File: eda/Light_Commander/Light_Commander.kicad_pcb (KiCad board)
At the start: 2 copper layers, 71 x 108 mm, 164 parts, among them J1 GATE0, J10 BUFFB, J11 BUFFC, J12 BUFFD, J13 Eurorack_Power, J14 USB_C_Receptacle_USB2.0_16P, J15 Conn_01x05, J16 MIDI_IN, J17 MIDI_THRU, J18 Conn_01x03, J19 Conn_02x07_Odd_Even, J2 GATE1, J20 Conn_02x03_Odd_Even, J3 GATE2, J4 GATE3, J5 INA, J6 INB, J7 INC, J8 IND, J9 BUFFA, Q1 MMBT3904, Q2 MMBT3904, Q3 MMBT3904, Q4 MMBT3904, Q5 Q_PMOS_GSD, Q6 Q_NMOS_GSD, Q7 Q_PMOS_GDS, SW1 RotaryEncoder_Switch, SW2 SW_Push, SW3 SW_DPDT_x2, SW4 SW_DPDT_x2, U1 STM32F446RETx, U10 6N137, U11 NXU0101GW, U2 TL084, U3 AD8544, U4 R-785.0-0.5, U5 AP2112K-3.3, U6 USBLC6-2SC6, U7 2.5V Ref, U8 NXU0101GW, U9 SH1106_OLED, Y1 8 MHz

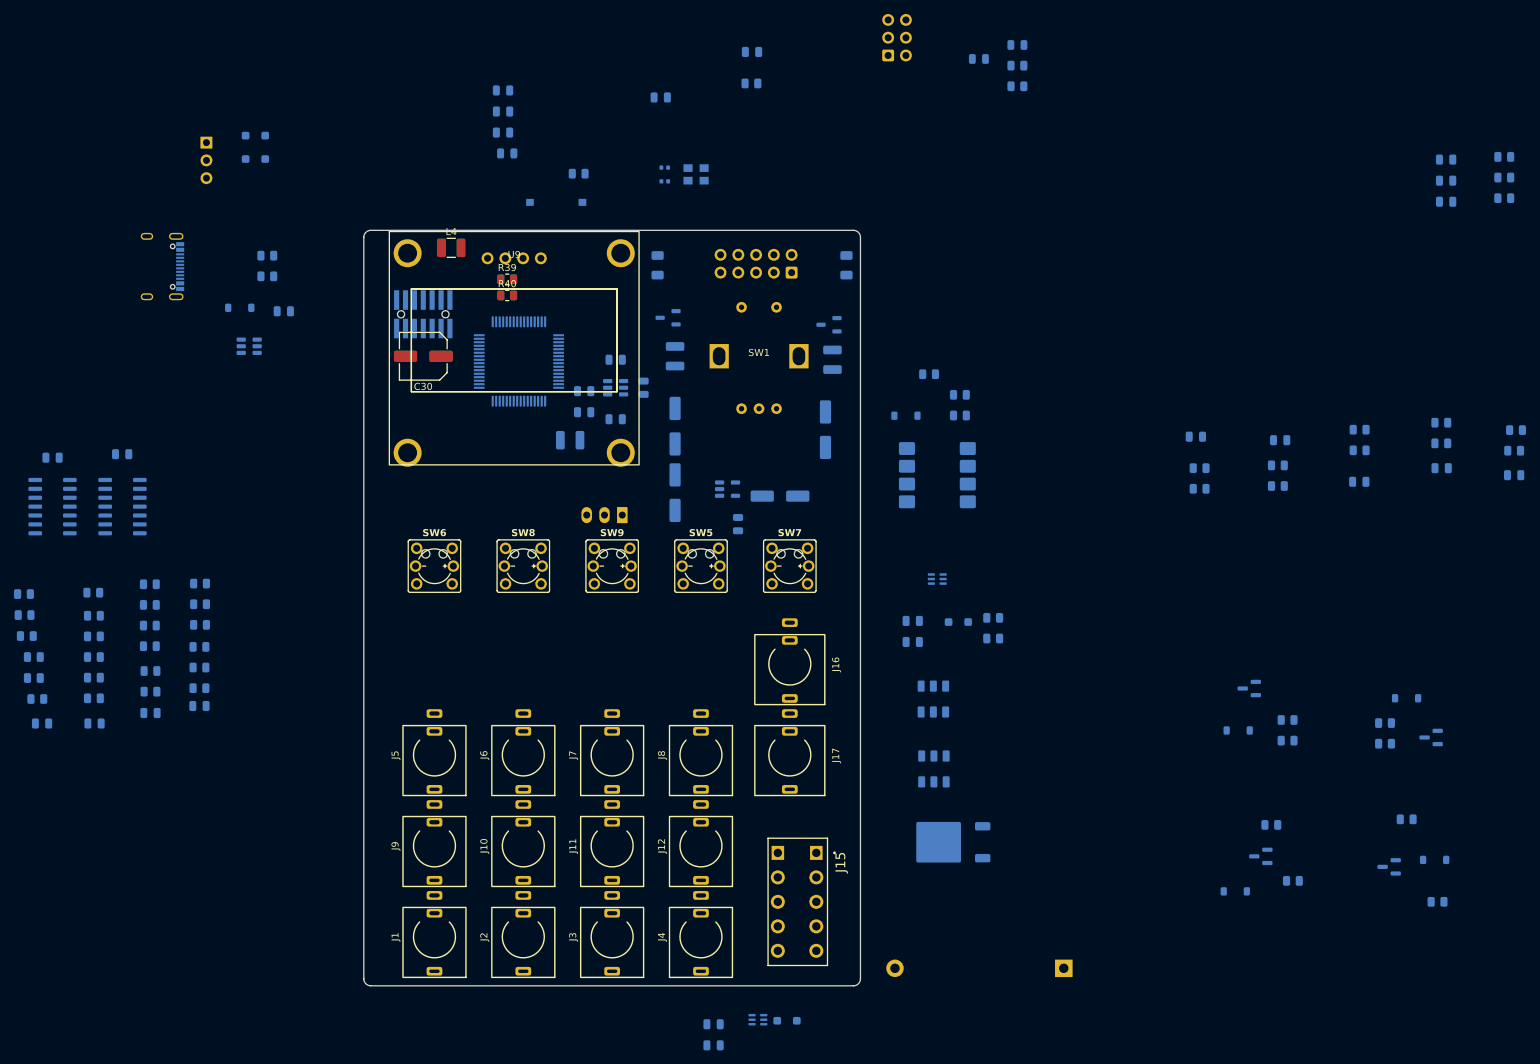
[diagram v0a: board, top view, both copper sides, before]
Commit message: Initial component placement
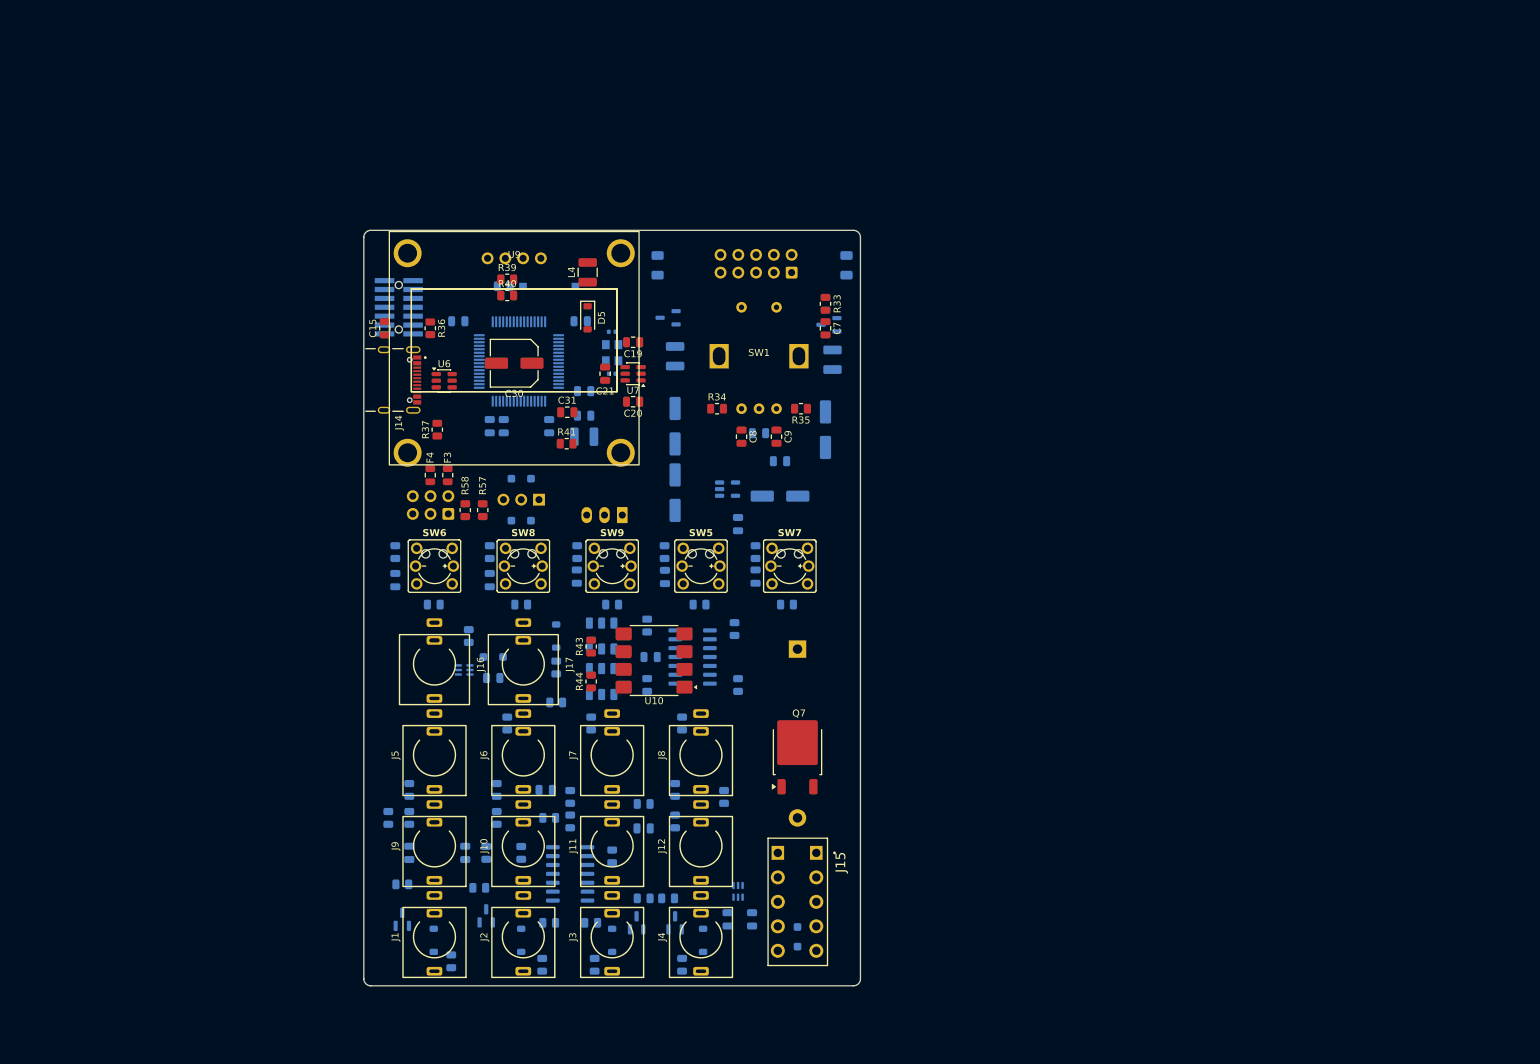
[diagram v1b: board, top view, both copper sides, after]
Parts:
- C15, C19, C20, C21, C31, C7, C8, C9, D5, F3, F4, J14, Q7, R33, R34, R35, R36, R37, R41, R43, R44, R57, R58, U10, U6, U7: moved to F.Cu
- moved Q1 149.4 mm to (70.0, 144.5), turned to 90 degrees
- moved D1 143.3 mm to (74.5, 147.5), turned to 90 degrees
- moved R26 141.9 mm to (70.0, 139.5), turned to 0 degrees
- moved R25 137.8 mm to (77.0, 150.5), turned to 90 degrees
- moved R30 120.8 mm to (97.5, 151.0), turned to 90 degrees
- moved D4 118.1 mm to (100.0, 147.5), turned to 90 degrees
- moved R28 117.5 mm to (81.0, 140.0), turned to 0 degrees
- moved R34 117.3 mm to (115.0, 71.5), turned to 0 degrees
- moved C35 116.3 mm to (69.0, 96.0), turned to -90 degrees
- moved R50 115.3 mm to (69.0, 92.0), turned to 90 degrees
- moved C37 114.8 mm to (82.5, 96.0), turned to -90 degrees
- moved Q2 113.8 mm to (82.0, 144.0), turned to 90 degrees
- moved R54 113.1 mm to (82.5, 92.0), turned to 90 degrees
- moved R56 112.8 mm to (95.0, 92.0), turned to 90 degrees
- moved C38 112.7 mm to (95.0, 95.5), turned to -90 degrees
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
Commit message: Start of trace routing
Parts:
- moved D5 23.8 mm to (76.0, 70.5), turned to 180 degrees
- moved C1 9.49 mm to (68.0, 126.0), turned to 90 degrees
- moved C2 9.22 mm to (81.0, 126.0), turned to 90 degrees
- moved R57 9.01 mm to (73.0, 89.0), turned to 0 degrees
- moved C21 7.50 mm to (106.5, 66.5)
- moved R9 5.22 mm to (83.5, 130.0)
- moved R42 4.27 mm to (93.5, 104.5), turned to 90 degrees
- moved C17 3.61 mm to (97.0, 64.5), turned to 180 degrees
- moved R40 3.50 mm to (88.5, 55.3)
- moved R23 3.20 mm to (107.0, 126.0), turned to 90 degrees
- moved C4 2.69 mm to (107.0, 130.5), turned to -90 degrees
- moved R11 2.50 mm to (81.0, 130.0)
- moved R45 2.00 mm to (81.5, 104.0)
- moved R41 1.58 mm to (93.0, 75.0), turned to 90 degrees
- moved Q6 1.05 mm to (132.1, 59.5), turned to 90 degrees
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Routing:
- net GND: track 0.00 -> 127.6 mm, vias 0 -> 51
- net +2V5: track 0.00 -> 107.6 mm, vias 0 -> 5
- net +3V3: track 0.00 -> 78.0 mm, vias 0 -> 23
- net Net-(U3A-+): track 0.00 -> 59.6 mm, vias 0 -> 1
- net Net-(U3B-+): track 0.00 -> 53.8 mm, vias 0 -> 2
- net INA_JACK: track 0.00 -> 41.0 mm, vias 0 -> 1
- net Net-(U3C-+): track 0.00 -> 40.1 mm, vias 0 -> 2
- net Net-(SW3A-C): track 0.00 -> 35.7 mm, vias 0 -> 2
- net I2C_SDA_EXPANDER: track 0.00 -> 34.6 mm
- net INC_JACK: track 0.00 -> 33.1 mm, vias 0 -> 1
- net BUFFA_JACK: track 0.00 -> 32.7 mm
- net INB_JACK: track 0.00 -> 32.5 mm, vias 0 -> 1
- net BUFFD_JACK: track 0.00 -> 31.6 mm
- net Net-(U3D-+): track 0.00 -> 30.6 mm, vias 0 -> 2
- net Net-(SW3A-A): track 0.00 -> 29.2 mm
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- added copper zone on In2.Cu, net +3V3
- added copper zone on F.Cu, net GND
- added copper zone on In1.Cu, net GND
- added copper zone on In2.Cu, net GND
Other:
- copper layers 2 -> 4

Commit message: More routing
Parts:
- R47, R49, R51, R53, R55: moved to F.Cu
- moved R47 7.85 mm to (118.1, 94.0), turned to 90 degrees
- moved R51 7.78 mm to (130.5, 94.0), turned to 90 degrees
- moved R53 7.71 mm to (92.4, 94.0), turned to 90 degrees
- moved R49 7.50 mm to (79.6, 94.0), turned to 90 degrees
- moved R55 7.43 mm to (105.0, 94.0), turned to 90 degrees
- moved U4 1.21 mm to (101.4, 85.5)
- moved R18 0.50 mm to (118.0, 103.0)
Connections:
- U1 pad 2: unconnected-(U1-PC13-Pad2) -> MIDI_BTN
- U1 pad 23: unconnected-(U1-PA7-Pad23) -> BACK_BTN
- U1 pad 27: unconnected-(U1-PB1-Pad27) -> MIDI_LED
- U1 pad 28: unconnected-(U1-PB2-Pad28) -> SETTINGS_LED
- U1 pad 33: unconnected-(U1-PB12-Pad33) -> FX_CHANGE_LED
- U1 pad 34: unconnected-(U1-PB13-Pad34) -> MOD_LED
- U1 pad 35: unconnected-(U1-PB14-Pad35) -> BACK_LED
- U1 pad 43: unconnected-(U1-PA10-Pad43) -> FX_CHANGE_BTN
- U1 pad 57: unconnected-(U1-PB5-Pad57) -> MOD_BTN
- U1 pad 58: unconnected-(U1-PB6-Pad58) -> SETTINGS_BTN
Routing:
- net MIDI_LED: track 0.00 -> 56.0 mm, vias 0 -> 1
- net FX_CHANGE_BTN: track 11.0 -> 58.4 mm, vias 0 -> 2
- net MIDI_BTN: track 10.9 -> 56.9 mm, vias 0 -> 1
- net SETTINGS_LED: track 0.00 -> 44.4 mm, vias 0 -> 1
- net SETTINGS_BTN: track 10.7 -> 53.5 mm, vias 0 -> 1
- net FX_CHANGE_LED: track 0.00 -> 40.0 mm, vias 0 -> 1
- net ENC_BTN: track 8.81 -> 48.2 mm, vias 0 -> 1
- net MOD_BTN: track 11.3 -> 46.0 mm, vias 0 -> 1
- net MOD_LED: track 0.00 -> 32.1 mm, vias 0 -> 2
- net BACK_LED: track 0.00 -> 29.8 mm, vias 0 -> 2
- net BACK_BTN: track 11.6 -> 36.9 mm
- net MIDI_OUT: track 0.00 -> 20.8 mm, vias 0 -> 1
- net MIDI_IN: track 27.8 -> 45.8 mm
- net +5V: track 17.8 -> 34.3 mm, vias 0 -> 3
- net Net-(SW6-LED+): track 9.91 -> 2.68 mm
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- removed copper zone on In2.Cu, net GND

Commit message: Switch to 6 layer board, use JLC06161H-7628 stackup, and continue routing
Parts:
- moved C26 2.92 mm to (98.5, 67.5)
- moved C27 2.92 mm to (98.5, 71.0)
- moved L3 2.92 mm to (98.5, 74.0)
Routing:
- net LED_SPI_RAW: track 1.51 -> 100.1 mm, vias 1 -> 2
- net -12V: track 16.3 -> 110.3 mm, vias 0 -> 2
- net +12V: track 18.6 -> 95.4 mm, vias 0 -> 3
- net IND_ADC: track 6.42 -> 70.1 mm, vias 2 -> 4
- net ENC_CH1: track 5.64 -> 61.5 mm, vias 0 -> 1
- net ENC_CH2: track 5.64 -> 56.7 mm, vias 0 -> 1
- net INA_ADC: track 4.25 -> 53.6 mm, vias 0 -> 2
- net INC_ADC: track 7.52 -> 56.0 mm
- net INB_ADC: track 4.46 -> 51.5 mm, vias 0 -> 2
- net +3V3: track 78.0 -> 110.5 mm, vias 23 -> 31
- net MIDI_IN: track 45.8 -> 76.6 mm
- net NRST: track 11.7 -> 36.5 mm, vias 1 -> 3
- net +5V: track 34.3 -> 22.1 mm
- net GND: track 127.6 -> 139.2 mm, vias 51 -> 56
- net MIDI_IN_PIN_5: track 13.7 -> 23.2 mm, vias 1 -> 3
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- added copper zone on F.Cu, net +5V
- added copper zone on In3.Cu, net GND
- added copper zone on In4.Cu, net GND
- removed copper zone on F.Cu, net GND
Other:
- copper layers 4 -> 6

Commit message: Route gate inputs
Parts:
- moved C30 2.55 mm to (86.5, 62.5), turned to -90 degrees
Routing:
- net GATE3_EXTI: track 2.60 -> 126.2 mm, vias 0 -> 3
- net GATE2_EXTI: track 2.60 -> 120.0 mm, vias 0 -> 4
- net GATE0_EXTI: track 4.10 -> 102.8 mm, vias 0 -> 2
- net GATE1_EXTI: track 3.10 -> 101.8 mm, vias 0 -> 2
- net LED_SPI_RAW: track 100.1 -> 96.5 mm
- net GND: track 139.2 -> 141.0 mm, vias 56 -> 55
- net IND_ADC: track 70.1 -> 69.3 mm
- net ENC_CH1: track 61.5 -> 60.9 mm

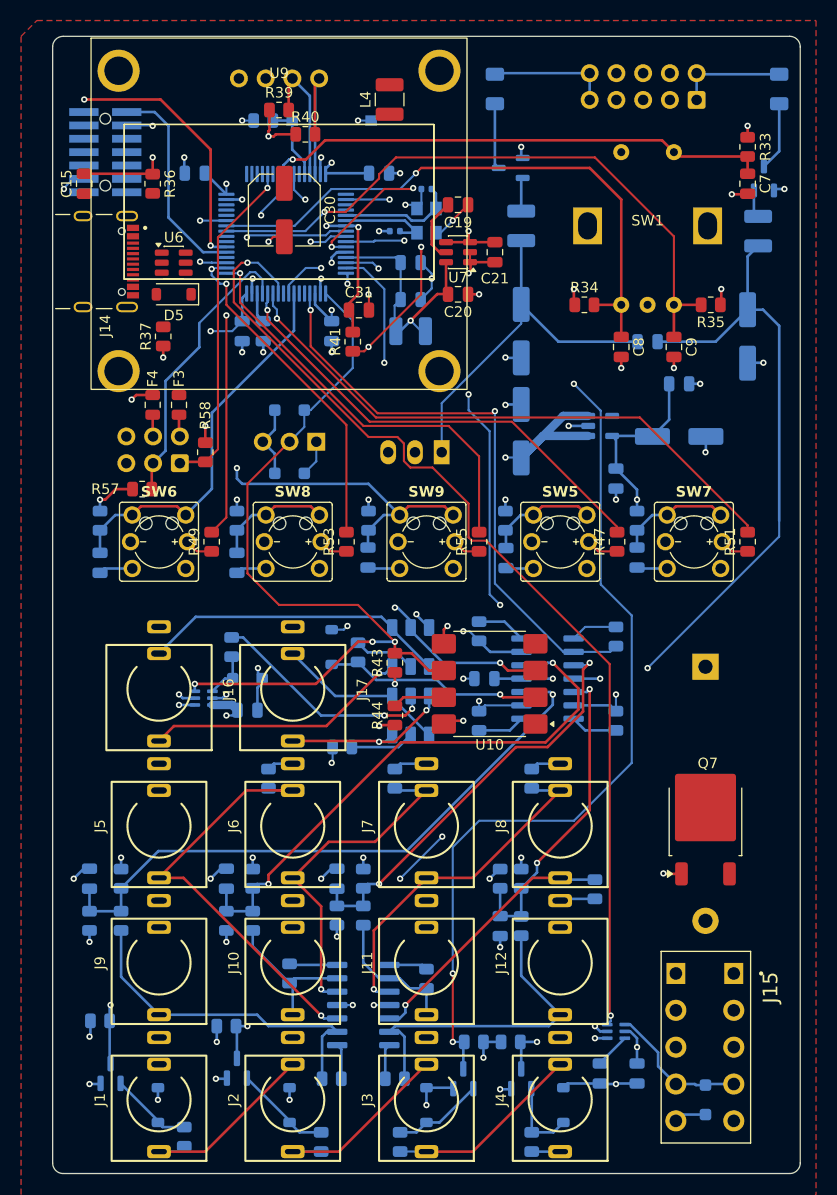
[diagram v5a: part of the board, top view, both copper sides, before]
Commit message: Route high current power for LED strip
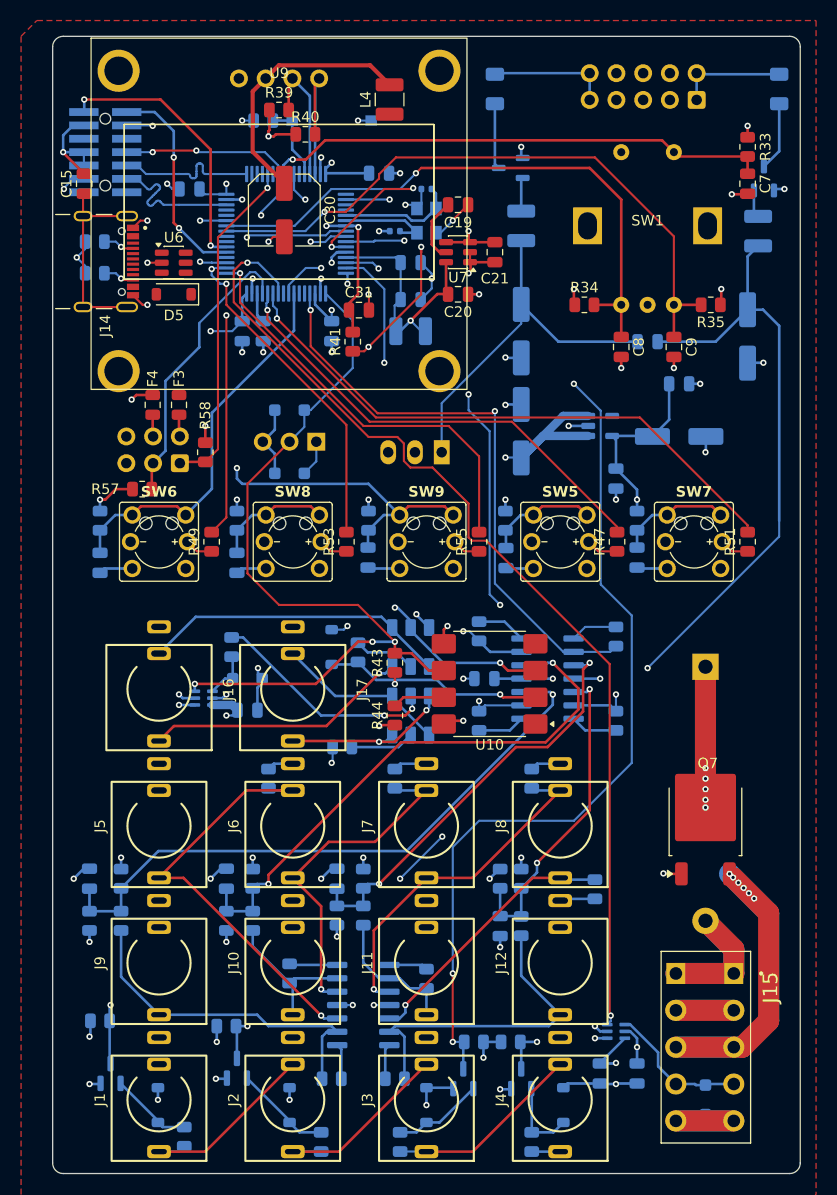
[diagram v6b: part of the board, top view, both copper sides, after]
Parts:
- R36, R37: moved to B.Cu
- moved R37 8.85 mm to (68.5, 68.5), turned to 0 degrees
- moved R36 7.78 mm to (68.5, 65.5), turned to 0 degrees
- moved C24 1.58 mm to (77.5, 60.5)
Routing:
- net +5V_LED: track 3.37 -> 162.8 mm, vias 0 -> 7
- net Net-(Q7-D): track 0.00 -> 80.2 mm, vias 0 -> 5
- net GND: track 141.0 -> 217.3 mm, vias 55 -> 58
- net Net-(J15-Pin_1): track 0.00 -> 69.7 mm
- net Net-(U9-VCC): track 0.00 -> 24.8 mm
- net Net-(J14-SHIELD): track 0.00 -> 19.2 mm
- net SWO: track 0.00 -> 15.8 mm, vias 0 -> 2
- net SWCLK: track 0.00 -> 13.9 mm
- net SWDIO: track 0.00 -> 13.8 mm
- net Net-(J14-CC2): track 0.00 -> 2.99 mm, vias 0 -> 1
- net Net-(J14-CC1): track 0.00 -> 2.99 mm, vias 0 -> 1
- net USART6_RX: track 24.6 -> 25.8 mm
- net USART6_TX: vias 0 -> 2

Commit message: Impedance controlled routing for USB signals
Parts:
- C30, D5, U6: moved to B.Cu
- F1: moved to F.Cu
- moved C30 19.3 mm to (104.5, 55.5)
- moved F1 4.50 mm to (111.0, 51.0)
- moved D5 2.24 mm to (77.0, 72.5), turned to 90 degrees
- moved Q5 2.06 mm to (110.0, 59.0), turned to 90 degrees
- moved U4 1.50 mm to (101.4, 87.0)
- moved U6 1.50 mm to (76.0, 66.0), turned to 90 degrees
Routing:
- net Net-(D5-A): track 0.00 -> 16.4 mm, vias 0 -> 2
- net Net-(J14-D--PadA7): track 0.00 -> 11.5 mm, vias 0 -> 1
- net Net-(U9-VCC): track 24.8 -> 33.7 mm, vias 0 -> 1
- net USB_D+: track 0.00 -> 7.17 mm
- net USB_D-: track 0.00 -> 5.58 mm
- net Net-(J14-D+-PadA6): track 0.00 -> 5.37 mm, vias 0 -> 1
- net GND: track 217.3 -> 222.6 mm, vias 58 -> 59
- net Net-(J13-Pin_10): track 11.6 -> 7.08 mm
- net LED_SPI_RAW: track 96.5 -> 98.1 mm
- net +5V: track 22.1 -> 23.5 mm, vias 3 -> 4
- net Net-(Q5-S): track 3.21 -> 2.48 mm
- net FX_CHANGE_BTN: track 58.4 -> 57.8 mm
- net Net-(Q5-D): track 6.25 -> 5.88 mm, vias 0 -> 1
